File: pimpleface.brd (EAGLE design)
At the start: 87.6 x 106.3 mm, 16 parts, among them J1 B06B-HCMKK

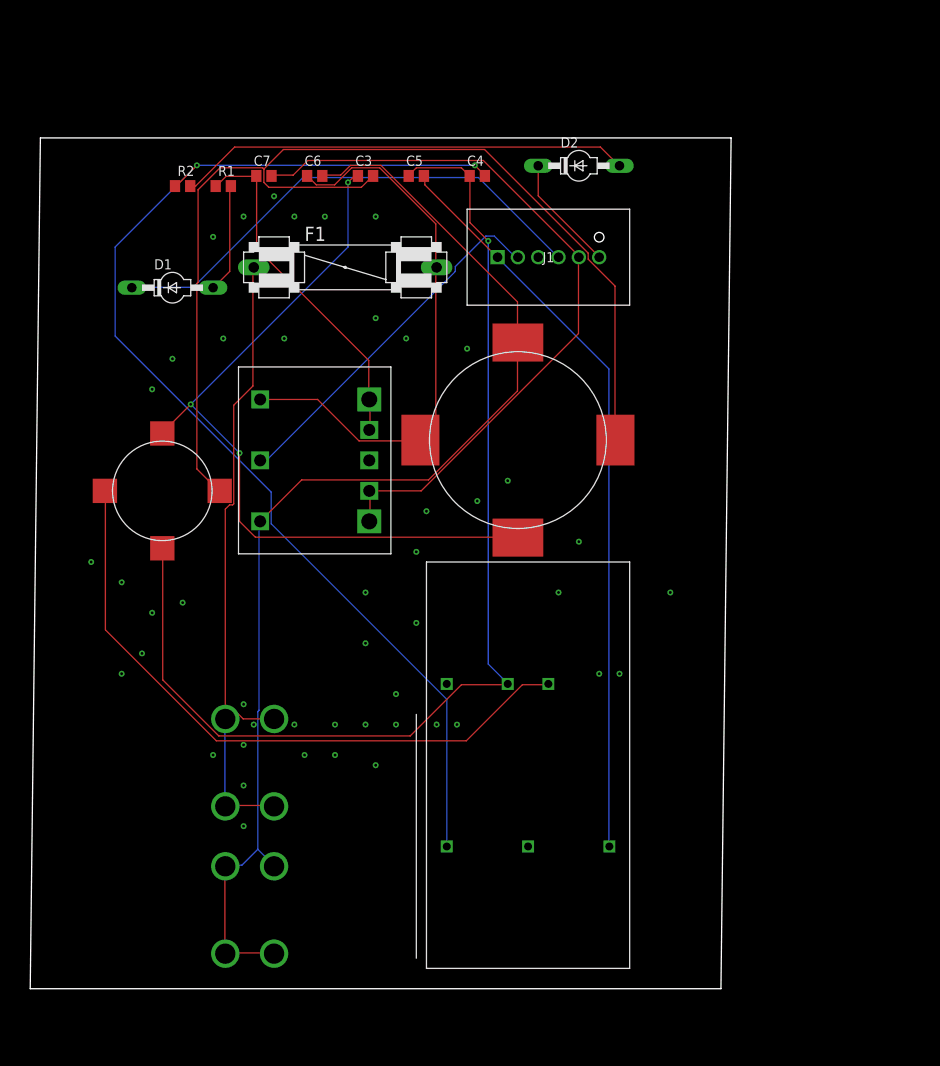
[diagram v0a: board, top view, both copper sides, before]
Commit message: Add files via upload
Autorouted shitty board. MVP.
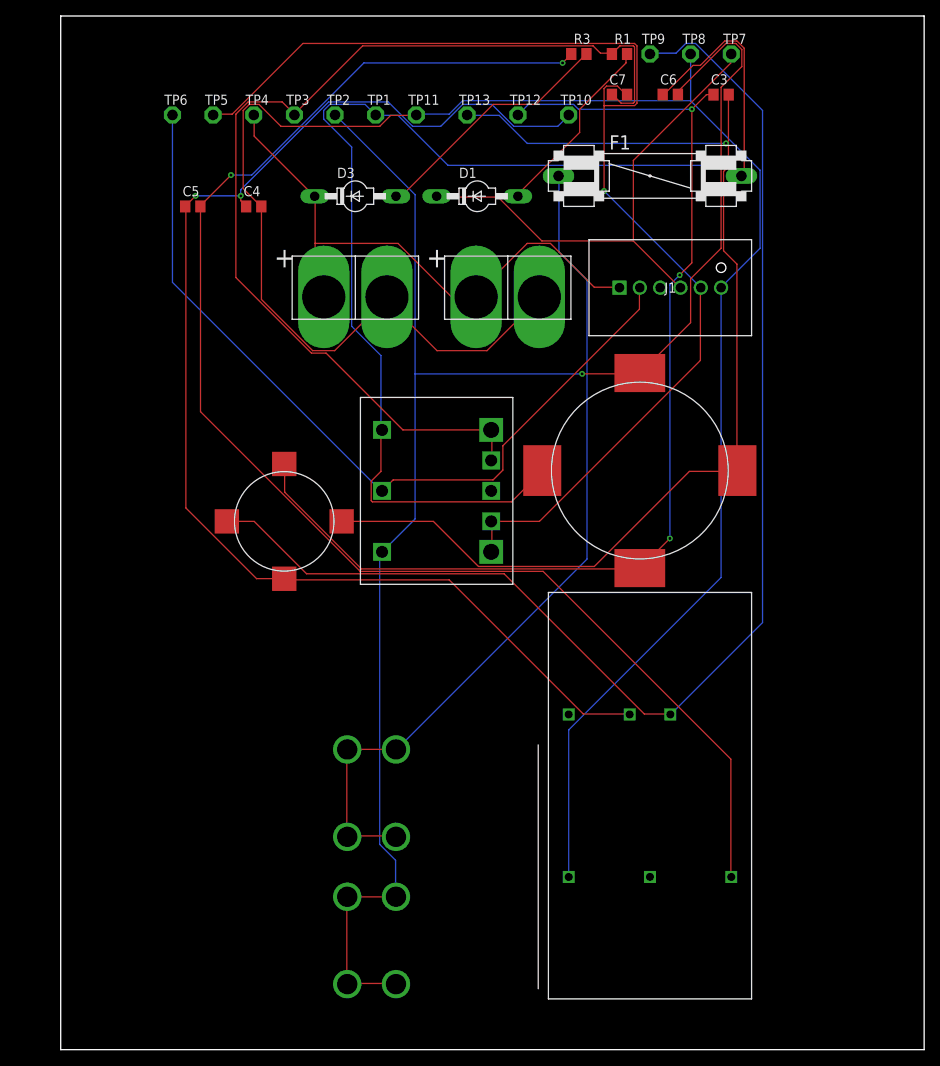
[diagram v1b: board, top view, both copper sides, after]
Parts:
- removed D2: BYV95, diode:SOD57-10
- removed R2: (no value), rcl:R0805
- added D3: BYV95, diode:SOD57-10
- added J2, J3: POWERPOLE_POWER45A_DRILL, powerpoles:POWERPOLE_PAIR_45A_HOLE
- added R3: (no value), rcl:R0805
- added TP1, TP10, TP11, TP12, TP13, TP2, TP3, TP4, TP5, TP6, TP7, TP8, TP9: TPPAD1-13, testpad:P1-13
- moved R1 52.2 mm to (71.1, 115.6)
- moved C7 45.6 mm to (71.1, 110.5)
- moved C3 45.6 mm to (83.8, 110.5)
- moved C6 45.6 mm to (77.5, 110.5)
- moved D1 39.8 mm to (53.3, 97.8)
- moved F1 39.8 mm to (74.9, 100.3)
- moved C4 28.2 mm to (25.4, 96.5)
- moved C5 28.2 mm to (17.8, 96.5)
- moved U$3 15.7 mm to (74.9, 22.9)
- moved J1 15.7 mm to (71.1, 86.4)
- moved U$4 15.7 mm to (29.2, 57.1)
- moved U$2 15.7 mm to (43.2, 14.0)
- moved BUCK150UH 15.7 mm to (73.7, 63.5)
- moved U$1 15.7 mm to (48.3, 61.0)
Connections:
- removed net N$12: D2.C, J1.6
- removed net N$13: D2.A, R2.2
- new net N$22: D3.C, J1.1, J2.RED, J3.RED, TP4.TP
- new net N$34: D3.A, R3.2
- net JIMGND: now also TP5.TP
- net LED: now also TP7.TP
- net N$1: now also TP3.TP
- net N$10: now also TP9.TP
- net N$11: now also TP2.TP
- net N$2: now also TP12.TP
- net N$3: now also TP1.TP
- net N$5: now also TP13.TP
- net N$7: now also TP10.TP
- net N$8: now also J1.6, J2.BLACK, J3.BLACK, TP11.TP, TP8.TP; no longer R2.1
- net N$9: now also R3.1; no longer J1.1
- net RC: now also TP6.TP
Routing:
- net N$8: track 146.9 -> 246.2 mm, vias 2 -> 0
- net N$3: track 70.5 -> 161.3 mm
- net N$1: track 43.4 -> 130.1 mm
- net N$9: track 93.5 -> 179.0 mm, vias 0 -> 2
- net N$10: track 81.5 -> 163.8 mm
- net N$22: track 0.00 -> 72.5 mm, vias 1 -> 0
- net N$11: track 148.5 -> 213.0 mm, vias 0 -> 1
- net RC: track 45.3 -> 104.0 mm
- net JIMGND: track 92.2 -> 149.1 mm, vias 0 -> 1
- net N$13: track 56.6 -> 0.00 mm
- net N$2: track 95.4 -> 138.1 mm
- net N$34: track 0.00 -> 31.2 mm
- net N$7: track 139.2 -> 163.5 mm, vias 1 -> 2
- net N$6: track 83.9 -> 106.4 mm
- net N$12: track 14.6 -> 0.00 mm
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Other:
- board size 87.6 x 106.3 mm -> 107.9 x 129.2 mm

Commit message: Add files via upload
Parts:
- removed C7: 10uF, rcl:C0805
- removed D1, D3: BYV95, diode:SOD57-10
- added C1: 10uF, rcl:EU25-10
- added LED1, LED2: (no value), led:CHIP-LED0603
- F1: value 7.5A -> FUSESHK20L; device special:FUSE -> fuse:SHK20L
- moved C5 116.7 mm to (90.7, 5.33)
- moved TP9 112.3 mm to (47.1, 6.76)
- moved C4 108.7 mm to (90.3, 9.33)
- moved TP10 106.9 mm to (85.6, 3.06)
- moved C3 103.3 mm to (33.3, 20.3), turned to 90 degrees
- moved TP11 101.6 mm to (54.8, 6.76)
- moved TP12 96.5 mm to (33.5, 14.8)
- moved TP13 85.7 mm to (33.4, 24.3)
- moved J3 84.1 mm to (92.5, 22.2), turned to 270 degrees
- moved R3 79.7 mm to (54.2, 36.8)
- moved U$2 75.7 mm to (9.58, 81.8)
- moved TP6 75.6 mm to (79.3, 67.8)
- moved BUCK150UH 72.0 mm to (16.1, 20.3), turned to 90 degrees
- moved TP4 69.2 mm to (79.5, 64.8)
- moved TP5 68.3 mm to (79.4, 73.8)
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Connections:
- net N$2 renamed TP-12
- net N$5 renamed TP13
- net N$8 renamed 1.6AGND
- removed net JIMGND: C7.2, J1.5, TP5.TP, U$1.-S, U$1.-VOUT
- removed net N$22: D3.C, J1.1, J2.RED, J3.RED, TP4.TP
- removed net N$34: D3.A, R3.2
- removed net N$4: D1.A, R1.2
- removed net N$6: F1.1, U$2.+1, U$2.+2, U$2.+3, U$2.+4
- new net 1.6AOUT: J1.1, J2.RED, J3.RED, LED1.C, R3.2, TP4.TP
- new net 6AGND: C1.2, J1.5, TP5.TP, U$1.-S, U$1.-VOUT
- new net FUSE: F1.1A, U$2.+1, U$2.+2, U$2.+3, U$2.+4
- net LED: now also LED2.C, R1.2; no longer D1.C
- net N$1: now also C1.1, LED2.A; no longer C7.1
- net N$3: now also F1.2A; no longer F1.2
- net N$9: now also LED1.A
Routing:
- net 1.6AGND: track 246.2 -> 56.1 mm, vias 0 -> 1
- net N$9: track 179.0 -> 3.37 mm, vias 2 -> 0
- net N$7: track 163.5 -> 0.00 mm, vias 2 -> 0
- net N$10: track 163.8 -> 6.22 mm
- net JIMGND: track 149.1 -> 0.00 mm, vias 1 -> 0
- net TP-12: track 138.1 -> 0.00 mm, vias 3 -> 0
- net 1.6AOUT: track 0.00 -> 108.7 mm
- net N$6: track 106.4 -> 0.00 mm
- net TP13: track 138.9 -> 38.2 mm, vias 1 -> 0
- net N$1: track 130.1 -> 30.4 mm
- net N$11: track 213.0 -> 139.1 mm
- net N$22: track 72.5 -> 0.00 mm
- net RC: track 104.0 -> 32.8 mm
- net N$3: track 161.3 -> 116.2 mm
- net LED: track 63.7 -> 27.2 mm
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- added copper zone on layer 16, net 1.6AGND
- added copper zone on layer 16, net 6AGND
- added copper zone on layer 1, net FUSE
- added copper zone on layer 1, net TP-12
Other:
- board size 107.9 x 129.2 mm -> 100 x 100 mm

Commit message: Add files via upload
Made new board and minor clean up of schematic. Still needs the LED fixed.
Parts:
- turned C5 to 180 degrees
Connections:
- net N$1 renamed +VOUT
- net TP-12 renamed N$24
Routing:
- net N$9: track 3.37 -> 83.5 mm
- net N$7: track 0.00 -> 78.6 mm
- net N$10: track 6.22 -> 50.7 mm
- net 6AGND: track 30.1 -> 8.67 mm
- net 1.6AGND: track 56.1 -> 68.4 mm
- net LED: track 27.2 -> 36.3 mm
- net +VOUT: track 30.4 -> 29.0 mm
- added copper zone on layer 1, net +VOUT
- added copper zone on layer 1, net TP-12
- removed copper zone on layer 1, net N$24
